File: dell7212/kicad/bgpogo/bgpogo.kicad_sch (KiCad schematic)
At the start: 16 parts, among them J1 Conn_02x13_Odd_Even, J2 USB1135-15-9-L-B_REVA1, J3 Conn_01x13, J4 PJ-019, J5 Conn_01x03, J6 Conn_01x13, J7 Conn_01x09, J8 PJ-104H, J9 Conn_01x03, U1 AZ1117-5.0

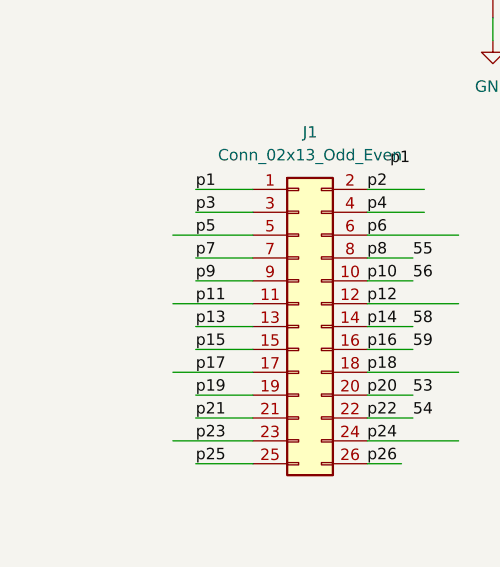
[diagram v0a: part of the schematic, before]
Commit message: ground plane, gnd not connected (bad).
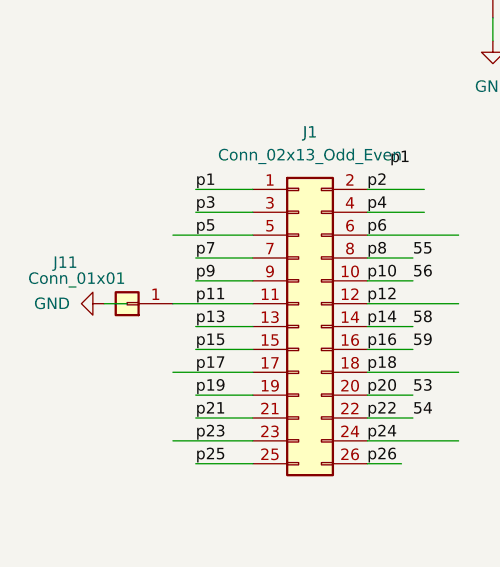
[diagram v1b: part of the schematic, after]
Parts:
- added J11: Conn_01x01, Connector_PinHeader_2.54mm:PinHeader_1x01_P2.54mm_Vertical, symbol Connector_Generic:Conn_01x01
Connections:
- net p11: now also J11.1 (Pin_1)
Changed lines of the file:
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@@
+	(wire
+		(pts
+			(xy 31.75 73.66) (xy 34.29 73.66)
+		)
+		(stroke
+			(width 0)
+			(type default)
+		)
+	)
 	(wire
 		(pts
@@
 	)
 	(symbol
+		(lib_id "Connector_Generic:Conn_01x01")
+		(at 34.29 73.66 180)
+		(unit 1)
+		(exclude_from_sim no)
+		(in_bom yes)
+		(on_board yes)
+		(dnp no)
+		(property "Reference" "J11"
+			(at 27.432 69.088 0)
+			(effects
+				(font
+					(size 1.27 1.27)
+				)
+			)
+		)
+		(property "Value" "Conn_01x01"
+			(at 28.702 70.866 0)
+			(effects
+				(font
+					(size 1.27 1.27)
+				)
+			)
+		)
+		(property "Footprint" "Connector_PinHeader_2.54mm:PinHeader_1x01_P2.54mm_Vertical"
+			(at 34.29 73.66 0)
+			(effects
+				(font
+					(size 1.27 1.27)
+				)
+				(hide yes)
+			)
+		)
+		(property "Datasheet" "~"
+			(at 34.29 73.66 0)
+			(effects
+				(font
+					(size 1.27 1.27)
+				)
+				(hide yes)
+			)
+		)
+		(property "Description" "Generic connector, single row, 01x01, script generated (kicad-library-utils/schlib/autogen/connector/)"
+			(at 34.29 73.66 0)
+			(effects
+				(font
+					(size 1.27 1.27)
+				)
+				(hide yes)
+			)
+		)
+		(pin "1"
+		)
+		(instances
+			(project "bgpogo"
+				(path "/32687b02-412d-4c2f-95b1-54c4396d397d"
+					(reference "J11")
+					(unit 1)
+				)
+			)
+		)
+	)
+	(symbol
 		(lib_id "Mechanical:MountingHole")
 		(at 158.75 54.61 0)
@@
 					(unit 1)
 				)
+			)
+		)
+	)
+	(symbol
+		(lib_id "power:GND")
+		(at 31.75 73.66 270)
+		(unit 1)
+		(exclude_from_sim no)
+		(in_bom yes)
+		(on_board yes)
+		(dnp no)
+		(fields_autoplaced yes)
+		(property "Reference" "#PWR04"
+			(at 25.4 73.66 0)
+			(effects
+				(font
+					(size 1.27 1.27)
+				)
+				(hide yes)
+			)
+		)
+		(property "Value" "GND"
+			(at 27.94 73.6599 90)
+			(effects
+				(font
+					(size 1.27 1.27)
+				)
+				(justify right)
+			)
+		)
+		(property "Footprint" ""
+			(at 31.75 73.66 0)
+			(effects
+				(font
+					(size 1.27 1.27)
+				)
+				(hide yes)
+			)
+		)
+		(property "Datasheet" ""
+			(at 31.75 73.66 0)
+			(effects
+				(font
+					(size 1.27 1.27)
+				)
+				(hide yes)
+			)
+		)
+		(property "Description" "Power symbol creates a global label with name \"GND\" , ground"
+			(at 31.75 73.66 0)
+			(effects
+				(font
+					(size 1.27 1.27)
+				)
+				(hide yes)
+			)
+		)
+		(pin "1"
+		)
+		(instances
+			(project "bgpogo"
+				(path "/32687b02-412d-4c2f-95b1-54c4396d397d"
+					(reference "#PWR04")
+					(unit 1)
+				)

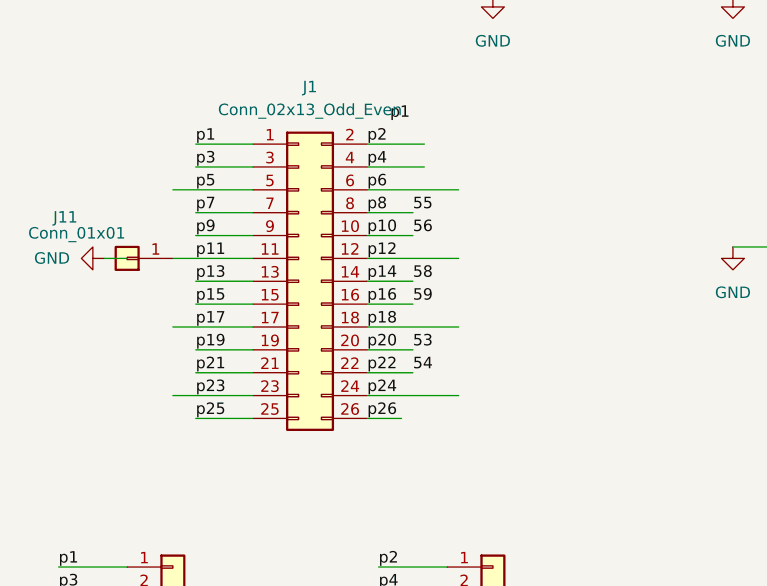
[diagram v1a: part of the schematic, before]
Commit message: ground pogos connected to GND via solder bridge. and bigger traces.
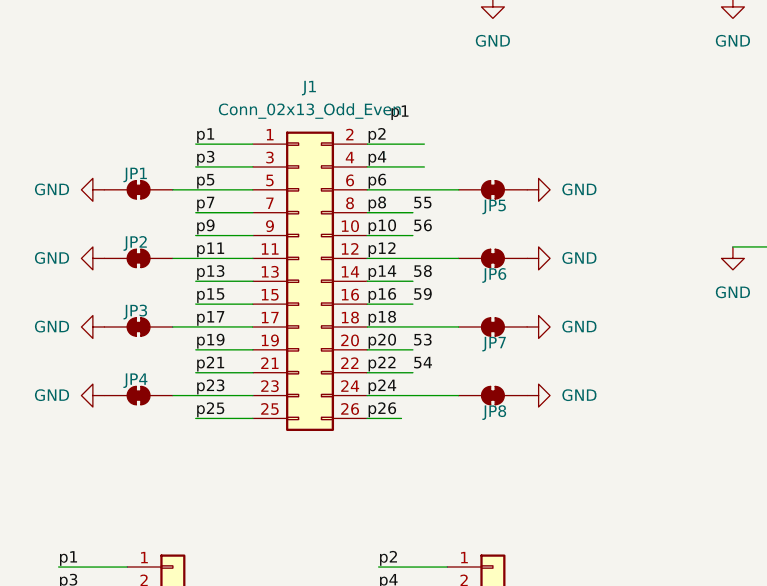
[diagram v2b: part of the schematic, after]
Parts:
- removed J11: Conn_01x01, Connector_PinHeader_2.54mm:PinHeader_1x01_P2.54mm_Vertical, symbol Connector_Generic:Conn_01x01
- added JP1, JP5: SolderJumper_2_Bridged, Jumper:SolderJumper-2_P1.3mm_Open_RoundedPad1.0x1.5mm, symbol Jumper:SolderJumper_2_Bridged
- added JP2, JP3, JP4, JP6, JP7, JP8: SolderJumper_2_Bridged, Jumper:SolderJumper-2_P1.3mm_Bridged_RoundedPad1.0x1.5mm, symbol Jumper:SolderJumper_2_Bridged
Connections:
- net GND: now also JP1.1 (A), JP2.1 (A), JP3.1 (A), JP4.1 (A), JP5.1 (A), JP6.1 (A), JP7.1 (A), JP8.1 (A)
- net p11: now also JP2.2 (B)
- net p12: now also JP6.2 (B)
- net p17: now also JP3.2 (B)
- net p18: now also JP7.2 (B)
- net p23: now also JP4.2 (B)
- net p24: now also JP8.2 (B)
- net p5: now also JP1.2 (B)
- net p6: now also JP5.2 (B)

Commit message: power nets, not really.
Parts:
- removed J4: PJ-019, libs:CUI_PJ-019, symbol PJ-019:PJ-019
- removed J5: Conn_01x03, Connector_PinHeader_2.54mm:PinHeader_1x03_P2.54mm_Vertical, symbol Connector_Generic:Conn_01x03
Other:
- moved on the sheet: J8, J9

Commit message: Power Now.
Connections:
- net p5: now also J8.2, J9.3 (Pin_3)
- net p6: now also J8.1, J9.1 (Pin_1)
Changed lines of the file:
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@@
 	)
 	(label "v+"
-		(at 123.19 115.57 0)
+		(at 125.73 115.57 0)
 		(effects
 			(font
@@
 	)
 	(label "v-"
-		(at 123.19 120.65 0)
-		(effects
-			(font
+		(at 125.73 120.65 0)
+		(effects
+			(font

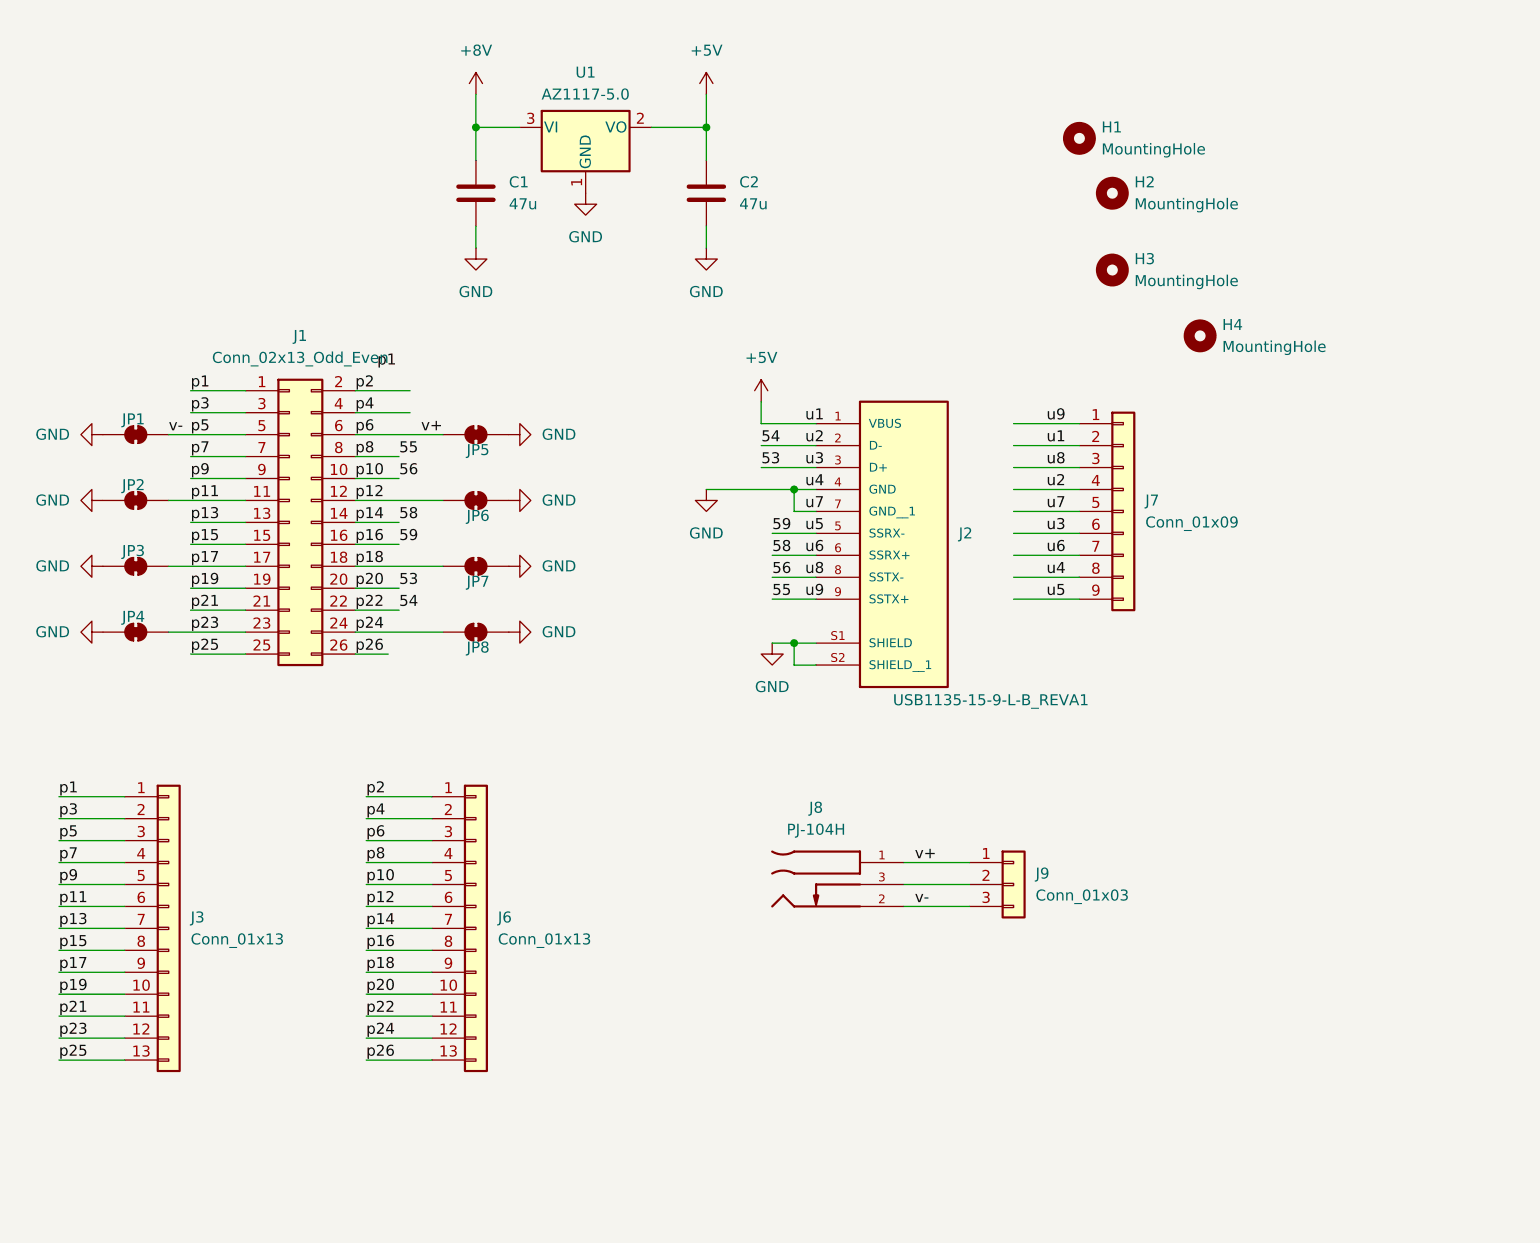
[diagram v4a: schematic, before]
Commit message: better power plug lables and header placement.
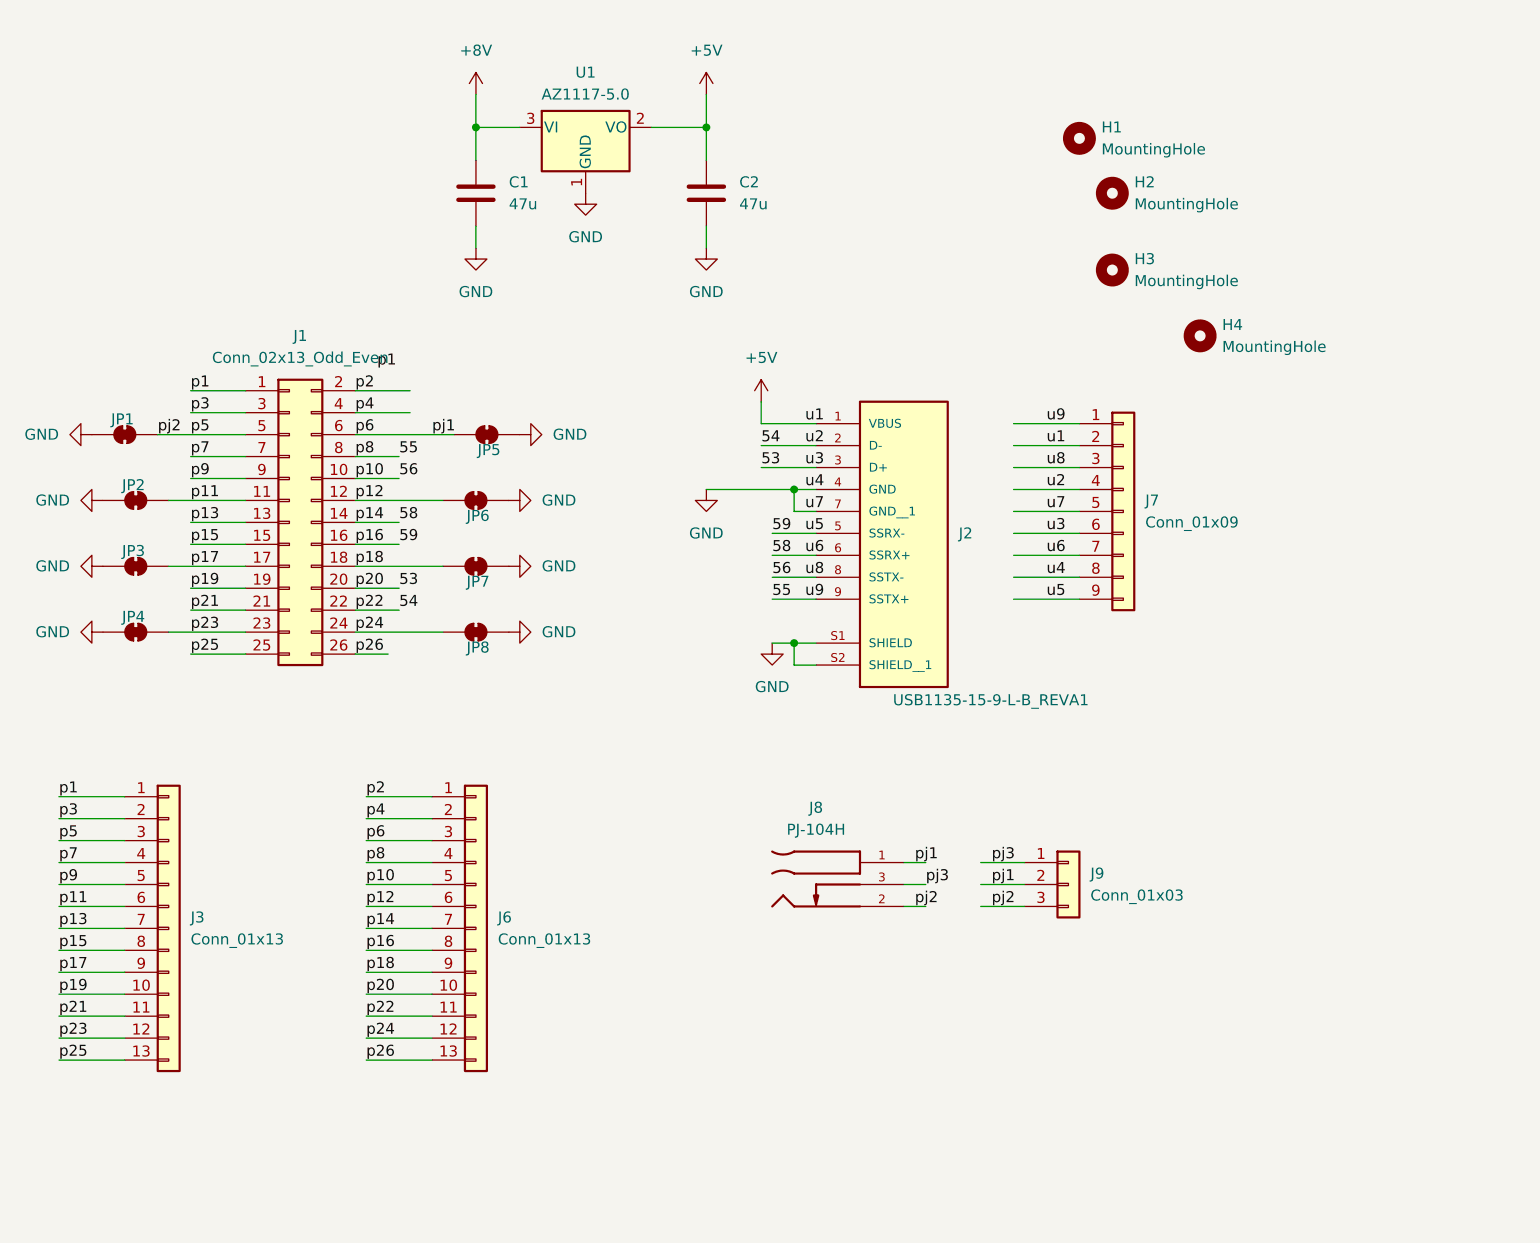
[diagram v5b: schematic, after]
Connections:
- net p6: now also J9.2 (Pin_2); no longer J9.1 (Pin_1)
- net pj3: now reaches J8.3
- net pj3: now also J9.1 (Pin_1); no longer J9.2 (Pin_2)
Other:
- moved on the sheet: J9, JP1, JP5

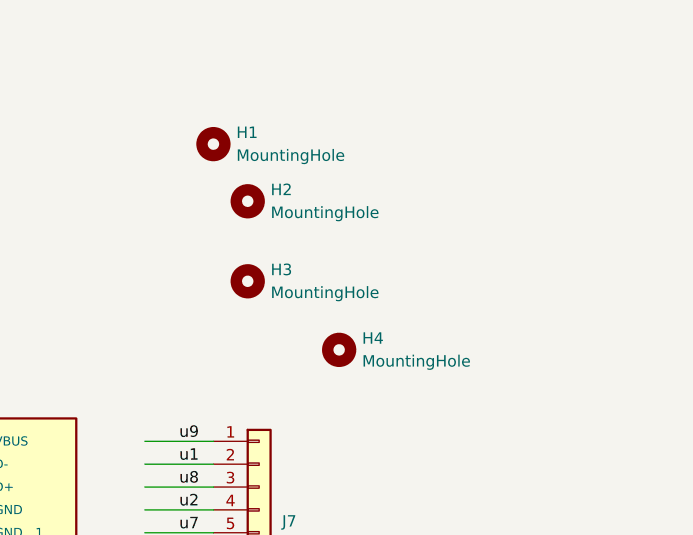
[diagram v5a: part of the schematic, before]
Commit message: ref image for back pack pogo mounting holes
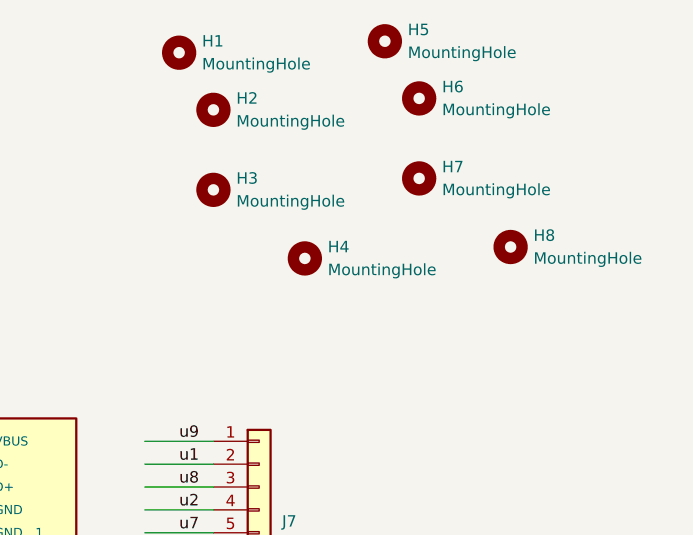
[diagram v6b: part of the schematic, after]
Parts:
- added H5, H6, H7, H8: MountingHole, MountingHole:MountingHole_2.5mm, symbol Mechanical:MountingHole
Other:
- moved on the sheet: H1, H2, H3, H4

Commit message: OIDIA
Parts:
- added J4: Conn_01x06, Connector_JST:JST_PH_S6B-PH-K_1x06_P2.00mm_Horizontal, symbol Connector_Generic:Conn_01x06
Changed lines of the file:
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@@
+	)
+	(symbol
+		(lib_id "Connector_Generic:Conn_01x06")
+		(at 116.84 140.97 0)
+		(unit 1)
+		(exclude_from_sim no)
+		(in_bom yes)
+		(on_board yes)
+		(dnp no)
+		(fields_autoplaced yes)
+		(property "Reference" "J4"
+			(at 119.38 140.9699 0)
+			(effects
+				(font
+					(size 1.27 1.27)
+				)
+				(justify left)
+			)
+		)
+		(property "Value" "Conn_01x06"
+			(at 119.38 143.5099 0)
+			(effects
+				(font
+					(size 1.27 1.27)
+				)
+				(justify left)
+			)
+		)
+		(property "Footprint" "Connector_JST:JST_PH_S6B-PH-K_1x06_P2.00mm_Horizontal"
+			(at 116.84 140.97 0)
+			(effects
+				(font
+					(size 1.27 1.27)
+				)
+				(hide yes)
+			)
+		)
+		(property "Datasheet" "~"
+			(at 116.84 140.97 0)
+			(effects
+				(font
+					(size 1.27 1.27)
+				)
+				(hide yes)
+			)
+		)
+		(property "Description" "Generic connector, single row, 01x06, script generated (kicad-library-utils/schlib/autogen/connector/)"
+			(at 116.84 140.97 0)
+			(effects
+				(font
+					(size 1.27 1.27)
+				)
+				(hide yes)
+			)
+		)
+		(pin "1"
+		)
+		(pin "2"
+		)
+		(pin "6"
+		)
+		(pin "3"
+		)
+		(pin "5"
+		)
+		(pin "4"
+		)
+		(instances
+			(project ""
+				(path "/32687b02-412d-4c2f-95b1-54c4396d397d"
+					(reference "J4")
+					(unit 1)
+				)
+			)
+		)
 	)
 	(symbol
